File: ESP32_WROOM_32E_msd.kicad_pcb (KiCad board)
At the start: 2 copper layers, 49.5 x 74 mm, 20 parts, among them J1 XH_6pin, J2 XH_6pin, J3 XH_2pin, J4 XH_2pin, SW1 SW_SPDT, U2 MCP2561-E-SN

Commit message: add mickey
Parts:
- added G***: LOGO, my_library:mickey, F.Cu at (101.5, 45.0)

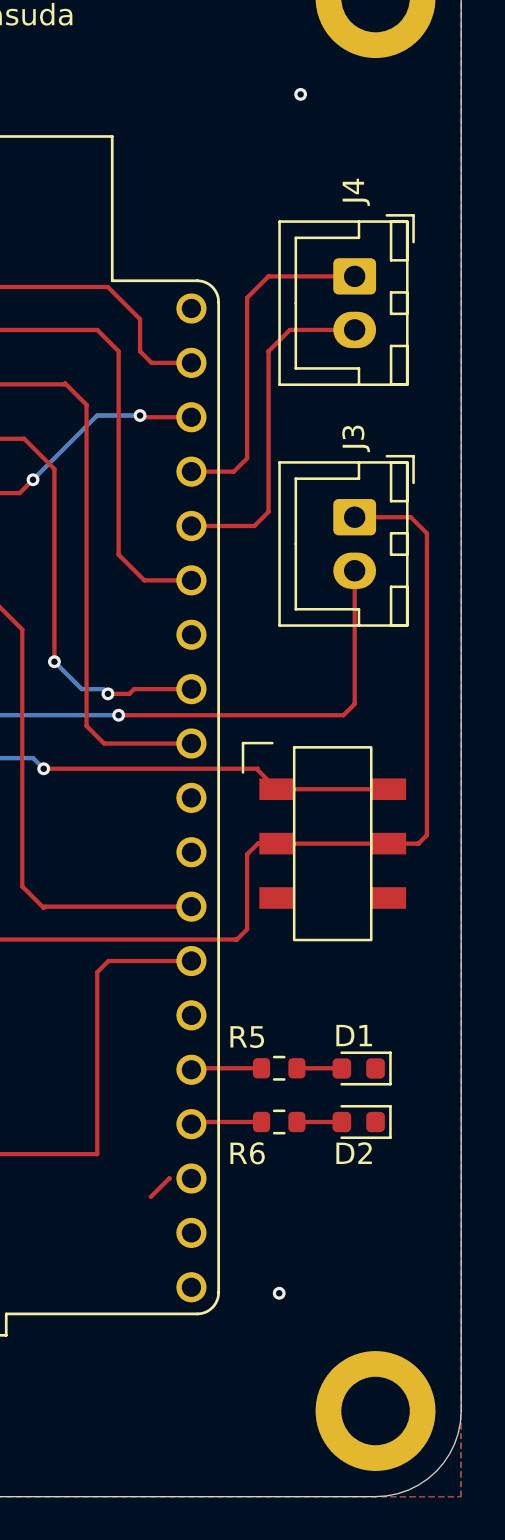
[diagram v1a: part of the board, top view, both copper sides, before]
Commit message: add encoder pin and motor driver pin
XH_4×4, pin header_8×1
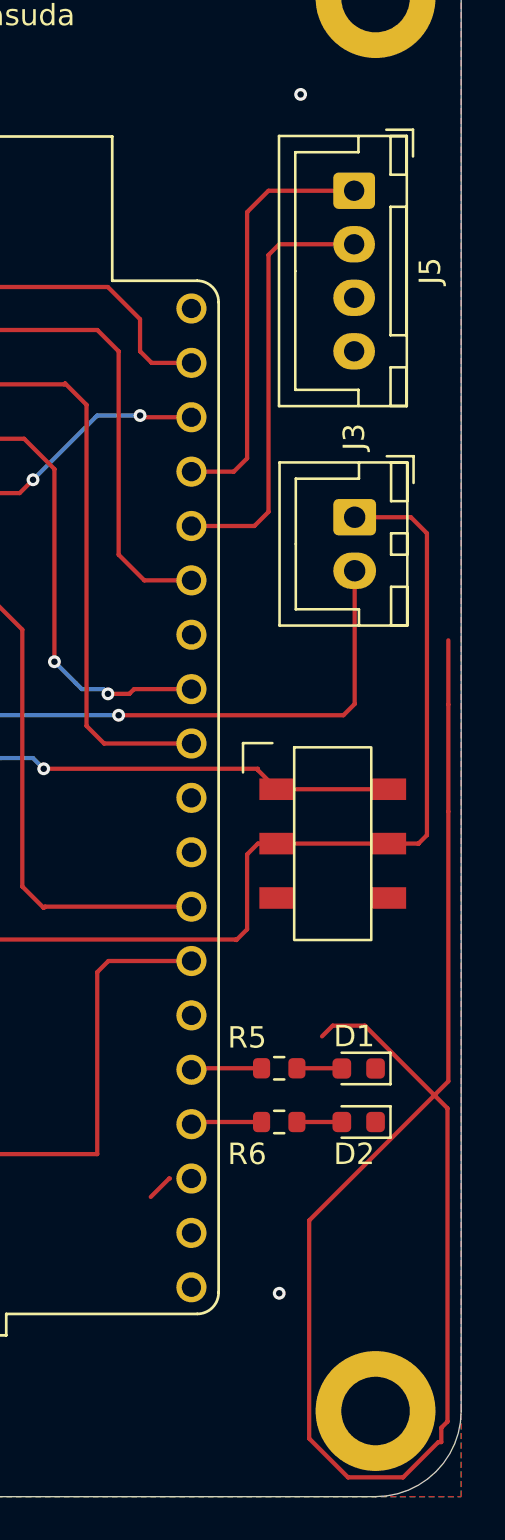
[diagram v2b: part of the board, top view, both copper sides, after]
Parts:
- removed J4: XH_2pin, Connector_JST:JST_XH_B2B-XH-A_1x02_P2.50mm_Vertical
- added J5: Conn_01x04_Socket, Connector_JST:JST_XH_B4B-XH-A_1x04_P2.50mm_Vertical, F.Cu at (130.5, 50.0)
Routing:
- net (no net): track 1.25 -> 72.2 mm
- net UART_RX: track 15.8 -> 20.1 mm
- net UART_TX: track 15.8 -> 19.8 mm

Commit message: almost complete
add Beta Ground,
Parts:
- removed G***: LOGO, my_library:mickey
- removed J3: XH_2pin, Connector_JST:JST_XH_B2B-XH-A_1x02_P2.50mm_Vertical
- added DC_motor1: DC_Motor, Connector_JST:JST_XH_B2B-XH-A_1x02_P2.50mm_Vertical, F.Cu at (100.2, 111.5)
- added J10: 7.5V, Connector_AMASS:AMASS_XT30PW-F_1x02_P2.50mm_Horizontal, F.Cu at (114.5, 108.5)
- added J9: Motor_Driver, Connector_PinHeader_2.54mm:PinHeader_1x08_P2.54mm_Vertical, F.Cu at (90.5, 93.2)
- added LB_Encoder1: LB_Encoder, Connector_JST:JST_XH_B4B-XH-A_1x04_P2.50mm_Vertical, F.Cu at (82.0, 89.5)
- added LF_Encoder1: LF_Encoder, Connector_JST:JST_XH_B4B-XH-A_1x04_P2.50mm_Vertical, F.Cu at (82.0, 61.2)
- added RB_Encoder1: RB_Encoder, Connector_JST:JST_XH_B4B-XH-A_1x04_P2.50mm_Vertical, F.Cu at (82.0, 103.5)
- added RF_Encoder1: RF_Encoder, Connector_JST:JST_XH_B4B-XH-A_1x04_P2.50mm_Vertical, F.Cu at (82.0, 75.2)
- added Servo_1: Servo_1, Connector_JST:JST_XH_B3B-XH-A_1x03_P2.50mm_Vertical, F.Cu at (130.5, 75.0)
- added Servo_2: Servo_2, Connector_JST:JST_XH_B3B-XH-A_1x03_P2.50mm_Vertical, F.Cu at (130.5, 86.5)
- CAN1: renamed from J5; value Conn_01x04_Socket -> CAN_External_Pin
- Motor_RL_B1: renamed from J2; value XH_6pin -> Motor_RL_B
- Motor_RL_F1: renamed from J1; value XH_6pin -> Motor_RL_F
- moved SW1 21.5 mm to (130.0, 102.0)
- moved D1 20.9 mm to (124.0, 110.8), turned to 90 degrees
- moved D2 19.6 mm to (121.5, 110.8), turned to 90 degrees
- moved R5 16.4 mm to (124.0, 107.1), turned to -90 degrees
- moved R6 14.6 mm to (121.5, 107.1), turned to -90 degrees
- moved CAN1 11.0 mm to (130.5, 61.0)
- moved H1 10.1 mm to (81.5, 112.5)
- moved H3 9.39 mm to (81.5, 45.0)
- moved Motor_RL_B1 9.00 mm to (90.5, 84.5)
- moved H2 5.50 mm to (131.5, 112.5)
- moved H4 4.00 mm to (131.5, 45.0)
- moved Motor_RL_F1 3.58 mm to (90.4, 64.9)
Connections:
- CAN1 pad 1: UART_TX -> CAN_H
- CAN1 pad 2: UART_RX -> CAN_L
- R2 pad 1: CAN_H -> Net-(SW1-A)
- U1 pad J3_10: unconnected-(U1-IO5-PadJ3_10) -> Servo1
- U1 pad J3_4: UART_TX -> unconnected-(U1-TXD0-PadJ3_4)
- U1 pad J3_5: UART_RX -> unconnected-(U1-RXD0-PadJ3_5)
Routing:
- net +5V: track 26.0 -> 175.2 mm, vias 2 -> 4
- net +7.5V: track 0.00 -> 95.3 mm
- net (no net): track 72.2 -> 0.00 mm
- net LF_PWM: track 43.0 -> 97.9 mm
- net LB_PWM: track 20.3 -> 63.9 mm, vias 0 -> 6
- net RF_PWM: track 45.7 -> 84.0 mm
- net Net-(SW1-A): track 25.1 -> 62.1 mm, vias 2 -> 4
- net CAN_H: track 57.8 -> 82.7 mm
- net UART_RX: track 20.1 -> 0.00 mm
- net UART_TX: track 19.8 -> 0.00 mm
- net LB_2: track 8.94 -> 27.7 mm, vias 0 -> 2
- net RB_2: track 31.9 -> 48.1 mm, vias 0 -> 1
- net RB_PWM: track 41.7 -> 56.4 mm, vias 0 -> 2
- net RF_1: track 34.2 -> 48.7 mm, vias 2 -> 3
- net LF_1: track 48.4 -> 62.7 mm, vias 0 -> 2
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- removed copper zone on F.Cu, net GND
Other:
- board size 49.5 x 74 mm -> 58 x 75.5 mm
- board text added: "Sugano Robocon 2024 A group Made by Ryutaro Masuda 2024/11/23"
- board text removed: "Sugano Robocon 2024 A group Made by Ryutaro Masuda 2024/11/16"

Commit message: complete ver2
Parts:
- SW1: footprint Original:slide_SW -> Connector_PinHeader_2.54mm:PinHeader_1x03_P2.54mm_Vertical
- moved SW1 5.52 mm to (130.5, 96.5)
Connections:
- H1 pad 1: GND -> unconnected-(H1-Pad1)
- H2 pad 1: GND -> unconnected-(H2-Pad1)
- H3 pad 1: GND -> unconnected-(H3-Pad1)
- H4 pad 1: GND -> unconnected-(H4-Pad1)
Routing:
- net GND: track 1.86 -> 62.9 mm, vias 0 -> 6
- added copper zone on F.Cu, net GND

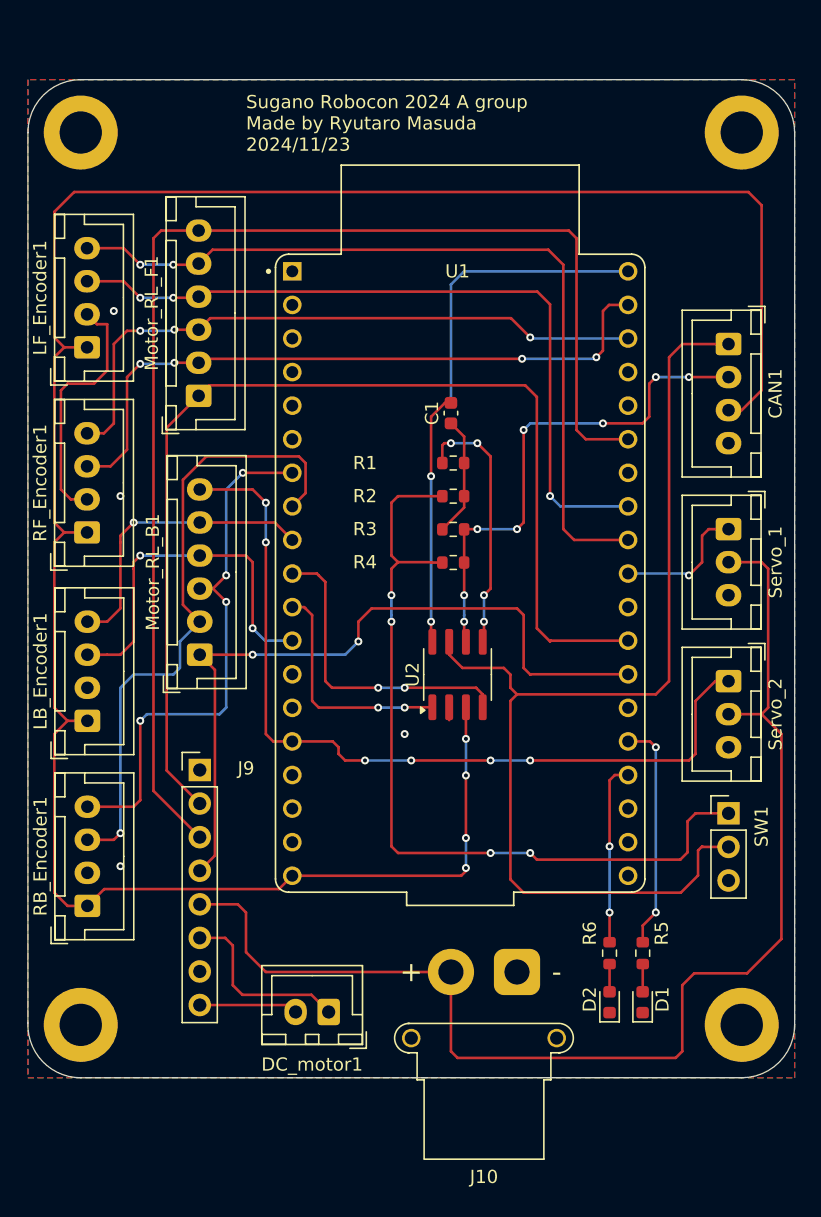
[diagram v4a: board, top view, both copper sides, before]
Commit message: revised wiring thickness
アクチュエータ部の配線太さを変更
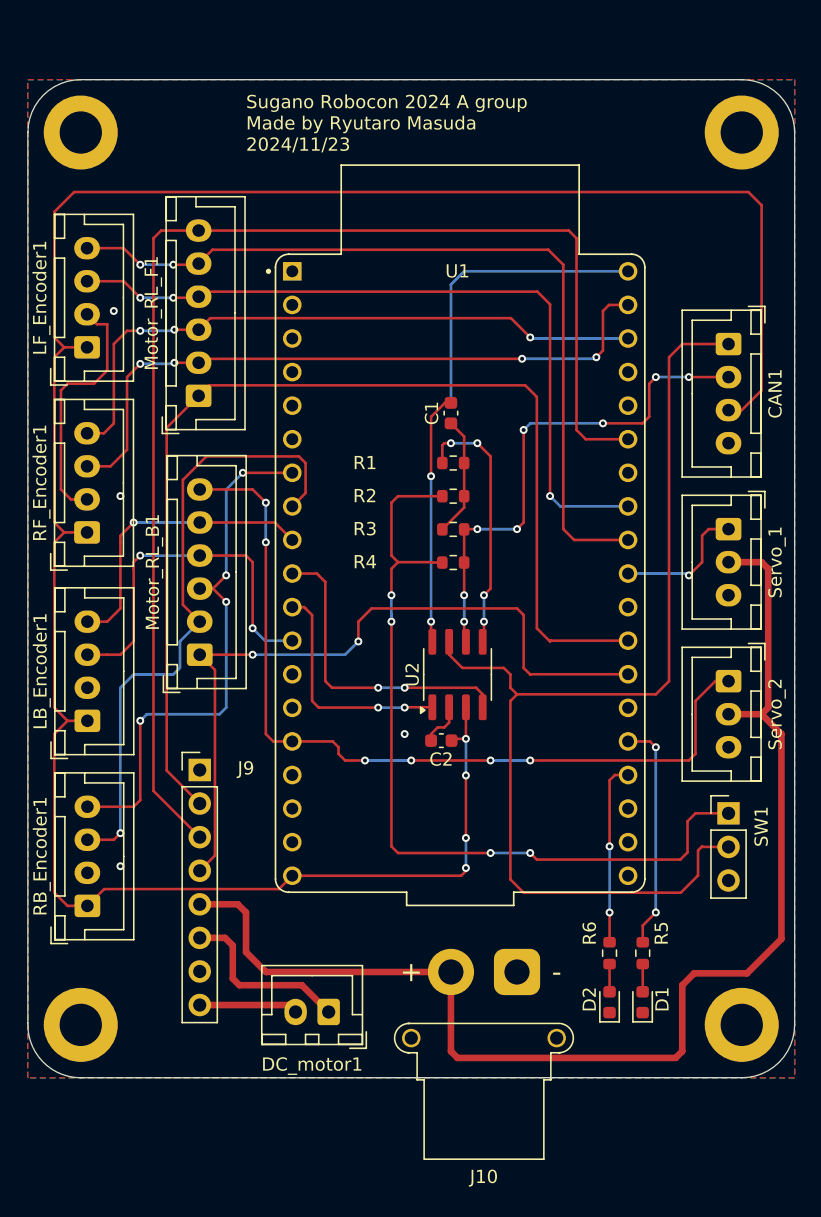
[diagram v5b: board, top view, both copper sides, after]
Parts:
- added C2: C, Capacitor_SMD:C_0603_1608Metric, F.Cu at (108.8, 91.0)
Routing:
- net GND: track 62.9 -> 65.3 mm
- net +5V: track 175.2 -> 176.3 mm
